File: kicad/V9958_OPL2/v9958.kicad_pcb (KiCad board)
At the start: 2 copper layers, 160 x 100.3 mm, 69 parts, among them J1 Audio, J2 RGB, J3 Composite, J4 S-VIDEO, P5 CONN_02X25, U1 74LS139, U10 Y3014B, U11 LM324, U12 cxa2075M, U2 V9958, U3 DRAM_64KX4, U4 DRAM_64KX4, U5 DRAM_64KX4, U6 DRAM_64KX4, U7 DRAM_64KX4, U8 YM3812, U9 DRAM_64KX4, X1 OSC, Y1 21,443Mhz

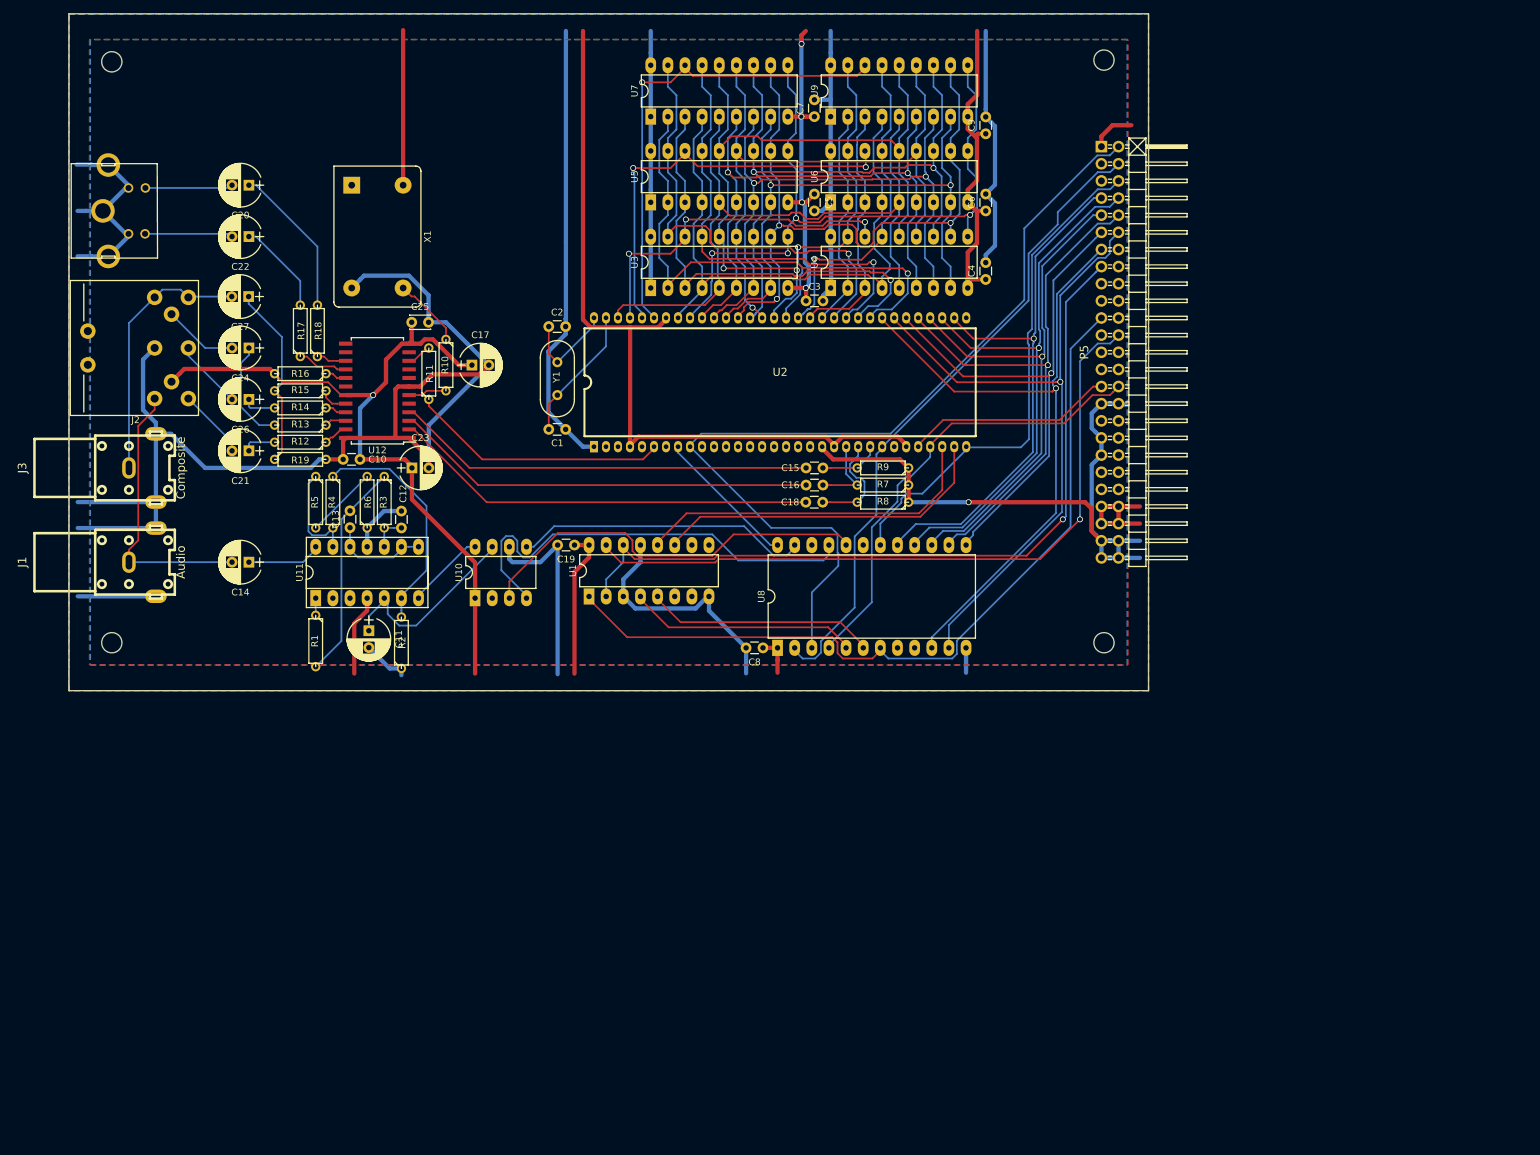
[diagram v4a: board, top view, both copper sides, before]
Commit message: DRC fixes, filled areas
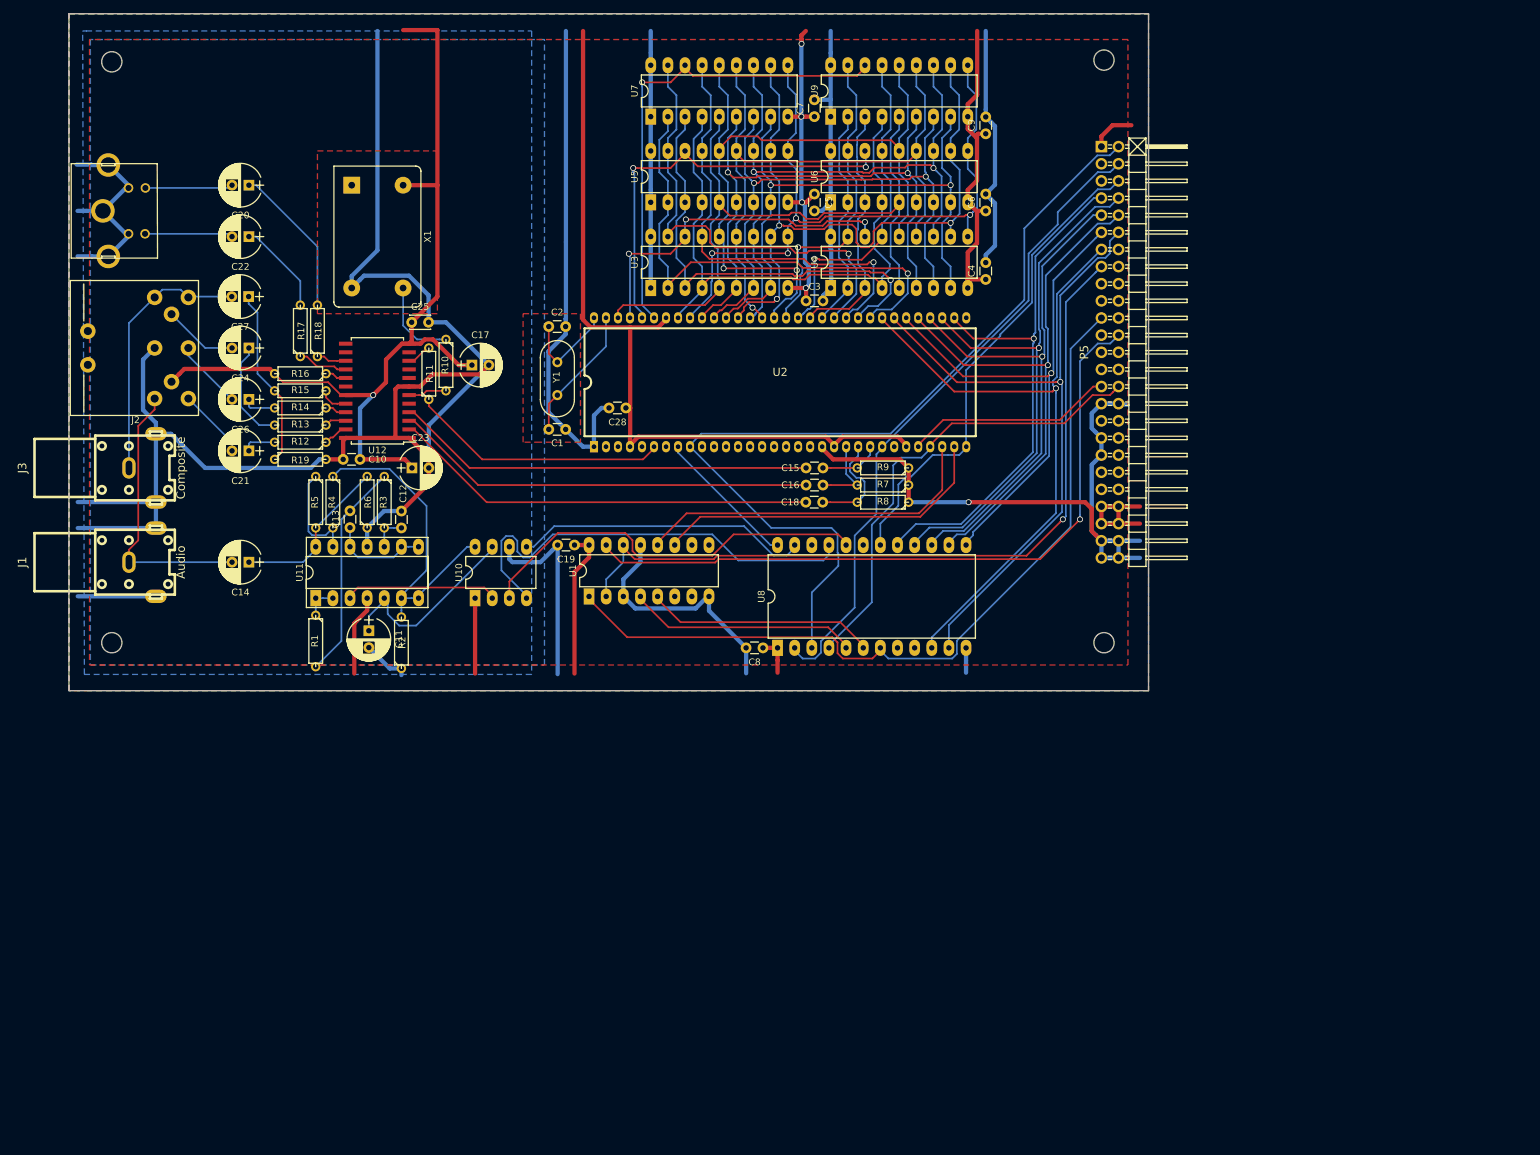
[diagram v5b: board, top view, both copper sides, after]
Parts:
- added C28: 100n, Capacitors_ThroughHole:C_Disc_D3.0mm_W1.6mm_P2.50mm, F.Cu at (144.8, 104.1)
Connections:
- U11 pad 2: Net-(U11-Pad2) -> Net-(R1-Pad1)
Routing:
- net GND: track 583.3 -> 638.4 mm
- net Net-(U10-Pad2): track 0.00 -> 22.9 mm
- net VCC: track 412.9 -> 422.4 mm
- net /D7: track 76.2 -> 72.6 mm
- net Net-(C14-Pad1): track 21.9 -> 24.7 mm
- net Net-(R2-Pad2): track 46.4 -> 49.0 mm
- net Net-(R1-Pad1): track 2.54 -> 5.08 mm
- net Net-(R10-Pad1): track 10.5 -> 12.8 mm
- net /A0: track 68.2 -> 69.6 mm
- net Net-(C27-Pad1): track 27.5 -> 26.6 mm
- added copper zone on F.Cu, net GND

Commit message: small improvements
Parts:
- U11: footprint Housings_DIP:DIP-14_W7.62mm_Socket_LongPads -> Housings_DIP:DIP-14_W7.62mm_LongPads
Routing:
- net /OPL_CLK: track 21.3 -> 20.8 mm

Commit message: RDY jumper
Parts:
- added JP1: JUMPER, Pin_Headers:Pin_Header_Straight_1x02_Pitch2.54mm, F.Cu at (203.8, 91.4)
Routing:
- net Net-(JP1-Pad2): track 0.00 -> 25.4 mm
- net RDY: track 0.00 -> 13.8 mm
- net /D7: track 72.6 -> 73.8 mm
- net /RESET: track 134.1 -> 133.0 mm

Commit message: fixes, optimizations
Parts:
- moved C23 24.7 mm to (108.0, 88.9)
- moved X1 21.6 mm to (119.4, 86.4), turned to 0 degrees
- moved C17 17.7 mm to (113.0, 113.0)
- moved R18 5.68 mm to (96.5, 87.6), turned to 180 degrees
- moved R10 5.24 mm to (119.4, 102.9), turned to 180 degrees
- moved R11 4.02 mm to (119.4, 97.8), turned to 180 degrees
- moved R17 2.54 mm to (96.5, 90.2), turned to 180 degrees
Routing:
- net GND: track 638.4 -> 559.4 mm
- net Net-(R10-Pad1): track 12.8 -> 29.9 mm
- net VCC: track 422.4 -> 412.0 mm
- net Net-(R2-Pad2): track 49.0 -> 39.5 mm
- net /CS_IO0: track 120.2 -> 112.7 mm, vias 0 -> 1
- net Net-(R18-Pad1): track 4.45 -> 11.1 mm
- net /RW: track 117.6 -> 113.3 mm
- net Net-(R4-Pad2): track 15.7 -> 11.5 mm
- net /CS_VDP: track 104.9 -> 100.8 mm
- net Net-(U10-Pad2): track 22.9 -> 26.5 mm
- net Net-(C20-Pad1): track 22.6 -> 19.2 mm
- net Net-(R10-Pad2): track 5.72 -> 3.18 mm
- net /CSYNC: track 38.6 -> 36.2 mm
- net Net-(R17-Pad1): track 7.52 -> 9.87 mm
- net /D0: track 100.5 -> 98.4 mm
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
